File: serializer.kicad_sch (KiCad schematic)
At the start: 22 parts, among them U301 STM32H723ZGTx

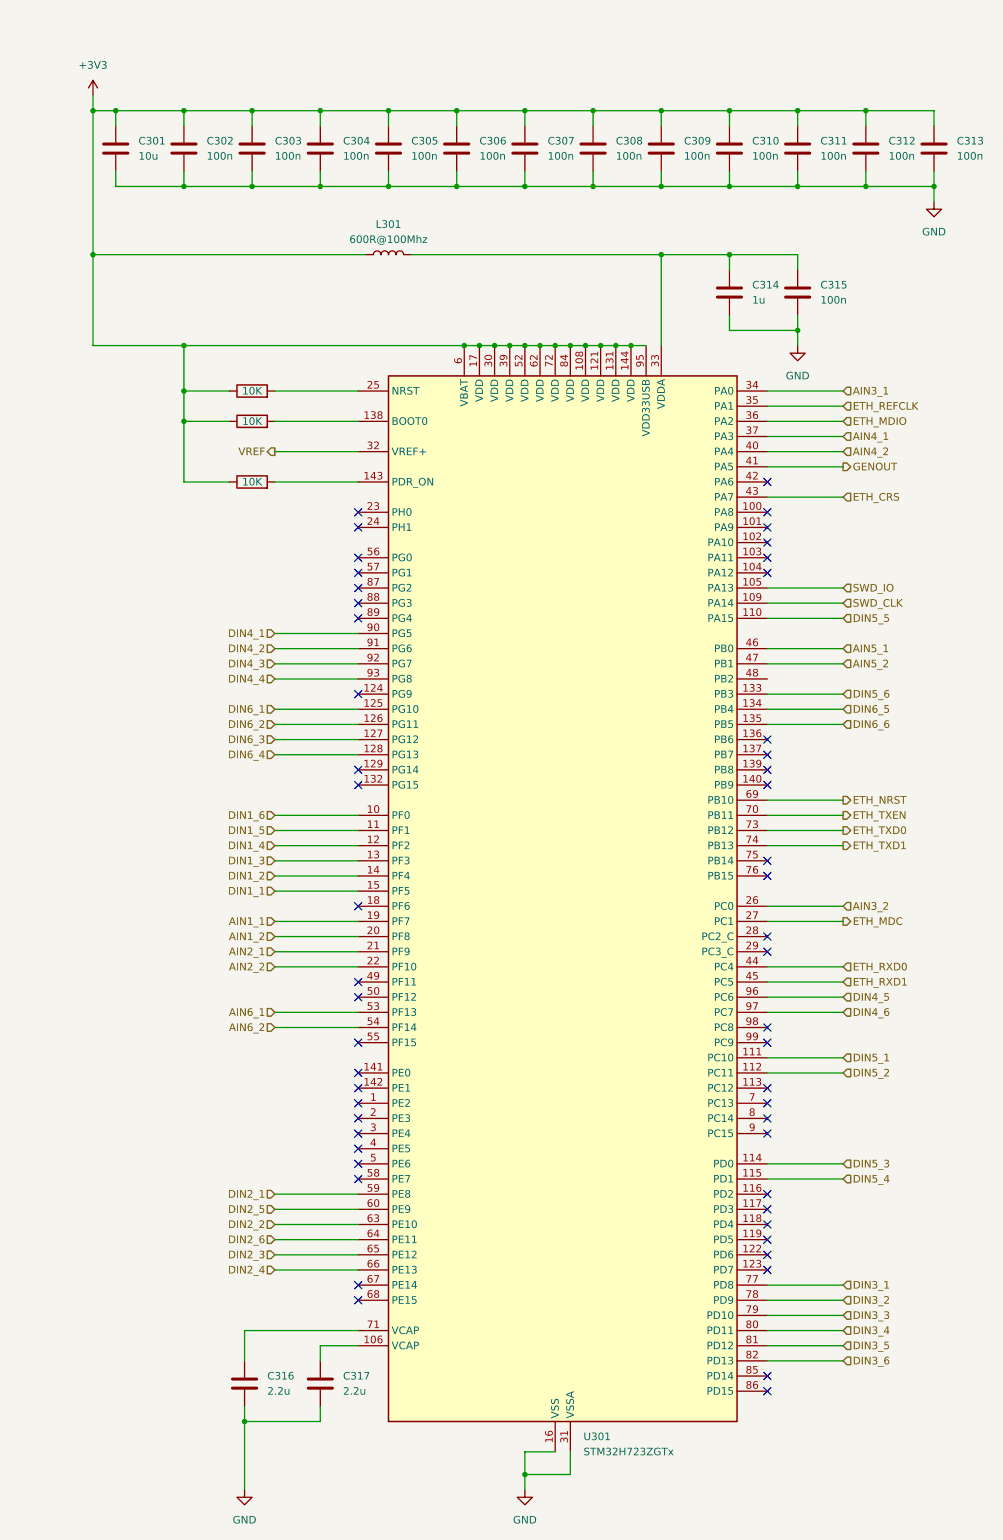
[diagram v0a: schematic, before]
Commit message: Merged receiver and transmitter
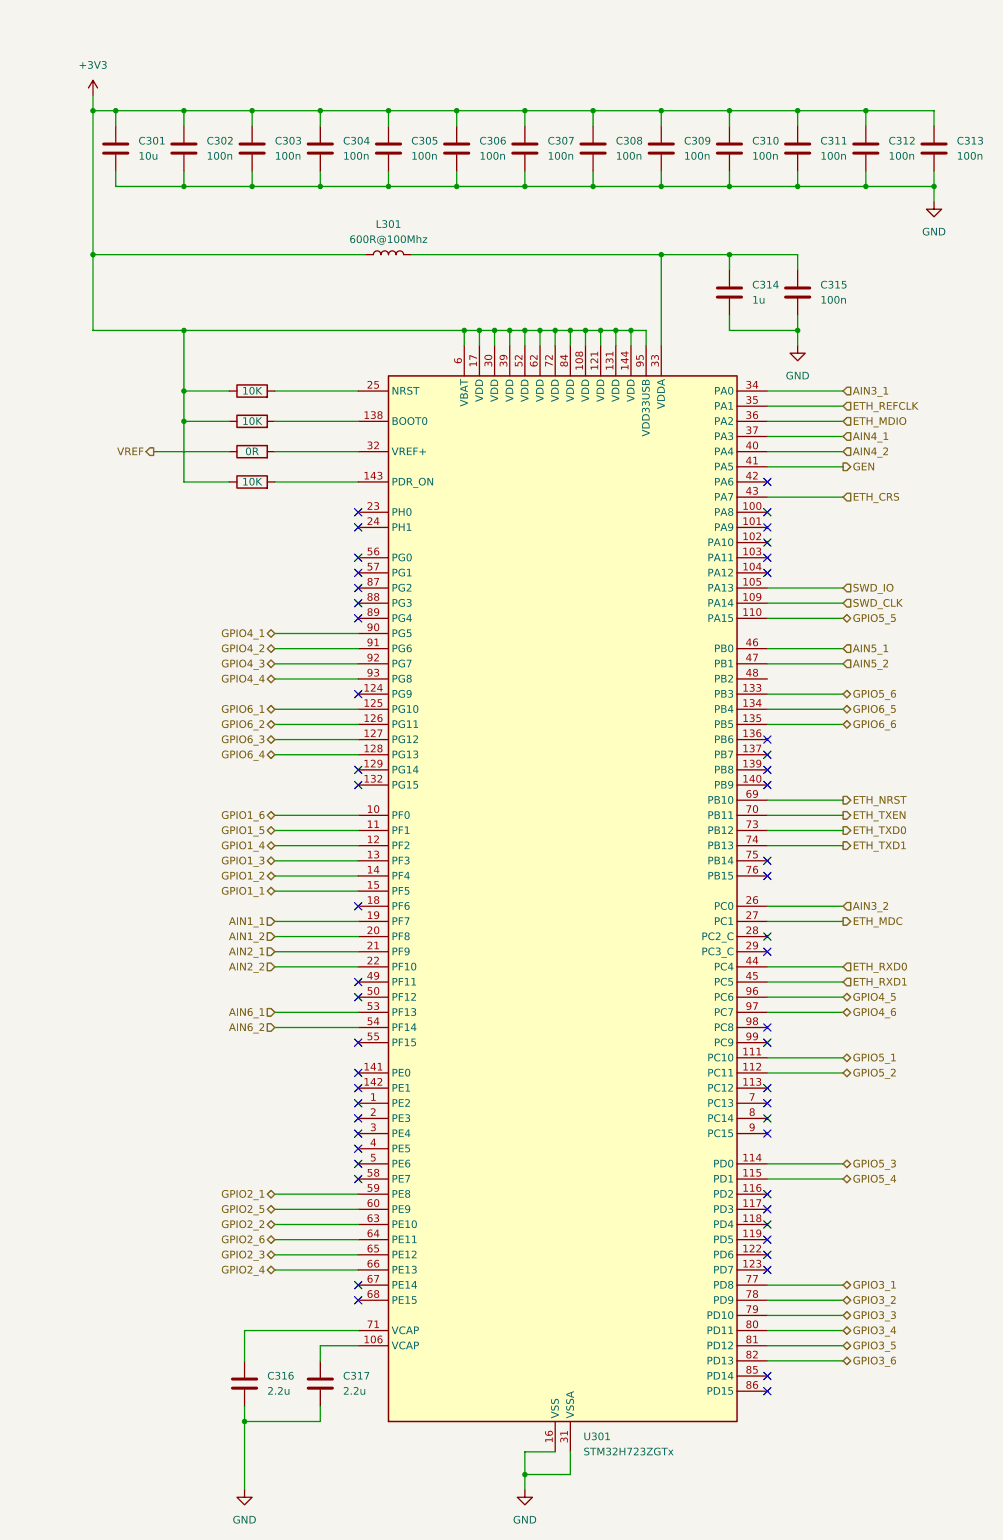
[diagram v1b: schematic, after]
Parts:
- added R303: 0R, Resistor_SMD:R_0603_1608Metric_Pad0.98x0.95mm_HandSolder, symbol Device:R
- renumbered R303 to R304
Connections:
- net VREF: now also R303.1; no longer U301.32 (VREF+)
- net DIN1_1 renamed GPIO1_1
- net DIN1_2 renamed GPIO1_2
- net DIN1_3 renamed GPIO1_3
- net DIN1_4 renamed GPIO1_4
- net DIN1_5 renamed GPIO1_5
- net DIN1_6 renamed GPIO1_6
- net DIN2_1 renamed GPIO2_1
- net DIN2_2 renamed GPIO2_2
- net DIN2_3 renamed GPIO2_3
- net DIN2_4 renamed GPIO2_4
- net DIN2_5 renamed GPIO2_5
- net DIN2_6 renamed GPIO2_6
- net DIN3_1 renamed GPIO3_1
- net DIN3_2 renamed GPIO3_2
- net DIN3_3 renamed GPIO3_3
- net DIN3_4 renamed GPIO3_4
- net DIN3_5 renamed GPIO3_5
- net DIN3_6 renamed GPIO3_6
- net DIN4_1 renamed GPIO4_1
- net DIN4_2 renamed GPIO4_2
- net DIN4_3 renamed GPIO4_3
- net DIN4_4 renamed GPIO4_4
- net DIN4_5 renamed GPIO4_5
- net DIN4_6 renamed GPIO4_6
- net DIN5_1 renamed GPIO5_1
- net DIN5_2 renamed GPIO5_2
- net DIN5_3 renamed GPIO5_3
- net DIN5_4 renamed GPIO5_4
- net DIN5_5 renamed GPIO5_5
- net DIN5_6 renamed GPIO5_6
- net DIN6_1 renamed GPIO6_1
- net DIN6_2 renamed GPIO6_2
- net DIN6_3 renamed GPIO6_3
- net DIN6_4 renamed GPIO6_4
- net DIN6_5 renamed GPIO6_5
- net DIN6_6 renamed GPIO6_6
- net GENOUT renamed GEN
- new net: R303.2, U301.32 (VREF+)

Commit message: Fixed ERC errors and warnings
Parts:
- added D301: LED Blue, Diode_SMD:D_0603_1608Metric_Pad1.05x0.95mm_HandSolder, symbol Device:LED
- added R303: 10K, Resistor_SMD:R_0603_1608Metric_Pad0.98x0.95mm_HandSolder, symbol Device:R
- renumbered R303 to R304, R304 to R305
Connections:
- net +3V3: now also D301.2 (A)
- net GND: now also R303.2
- new net: D301.1 (K), R303.1
- no-connect marks 52 -> 53

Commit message: Split schematic into three subprojects
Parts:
- renumbered C301 to C1, C310 to C10, C311 to C11, C312 to C12, C313 to C13, C314 to C14, C315 to C15, C316 to C16, C317 to C17, C302 to C2, C303 to C3, C304 to C4, C305 to C5, C306 to C6, C307 to C7, C308 to C8, C309 to C9, D301 to D1, L301 to L1, R301 to R1, R302 to R2, R303 to R3, R304 to R4, R305 to R5, U301 to U1

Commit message: Updated designators positions
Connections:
- net GND: now also R3.1; no longer R3.2
- net at D1.1 (K): now also R3.2; no longer R3.1

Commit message: Set capacitor and resistor values on tranciever circuits
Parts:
- C1: value 10u -> 10uF
- C10, C11, C12, C13, C15, C2, C3, C4, C5, C6, C7, C8, C9: value 100n -> 100nF
- C14: value 1u -> 1uF
- C16, C17: value 2.2u -> 2.2uF

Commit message: Assigned footprints for digital components
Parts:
- U1: value STM32H723ZGTx -> STM32H723ZGT

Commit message: Optimized components by cost and footprint size
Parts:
- renumbered C8 to C10, C9 to C11, C10 to C12, C14 to C13, C11 to C14, C12 to C16, C13 to C17, C16 to C3, C3 to C4, C4 to C5, C17 to C6, C5 to C7, C6 to C8, C7 to C9, R3 to R1, R1 to R2, R2 to R3

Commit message: Excluded rare components
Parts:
- removed C11, C17: 100nF, Capacitor_SMD:C_0603_1608Metric_Pad1.08x0.95mm_HandSolder, symbol Device:C
- added C2, C4, C7: 100nF, Capacitor_SMD:C_0603_1608Metric_Pad1.08x0.95mm_HandSolder, symbol Device:C
- renumbered C7 to C11, C8 to C13, C9 to C15, C13 to C17, C15 to C18, C2 to C3, C3 to C5, C4 to C6, C6 to C8, C5 to C9
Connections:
- net +3V3: now also L1.2, C2.1, C4.1, C7.1; no longer L1.1
- net GND: now also C2.2, C4.2, C7.2
- net at C17.1, C18.1, U1.33 (VDDA): now also L1.1; no longer L1.2
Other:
- moved on the sheet: C1, C11, C13, C15, C17, C18, C3, C6, C9, D1, R1
